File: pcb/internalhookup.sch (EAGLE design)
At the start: 8 parts, among them CN1 LASER, J1 CONTROL, J2 SERVO, J4 AZIMUTH, Q2 SMMBT2222ALT, U1 AMS1117-3.3

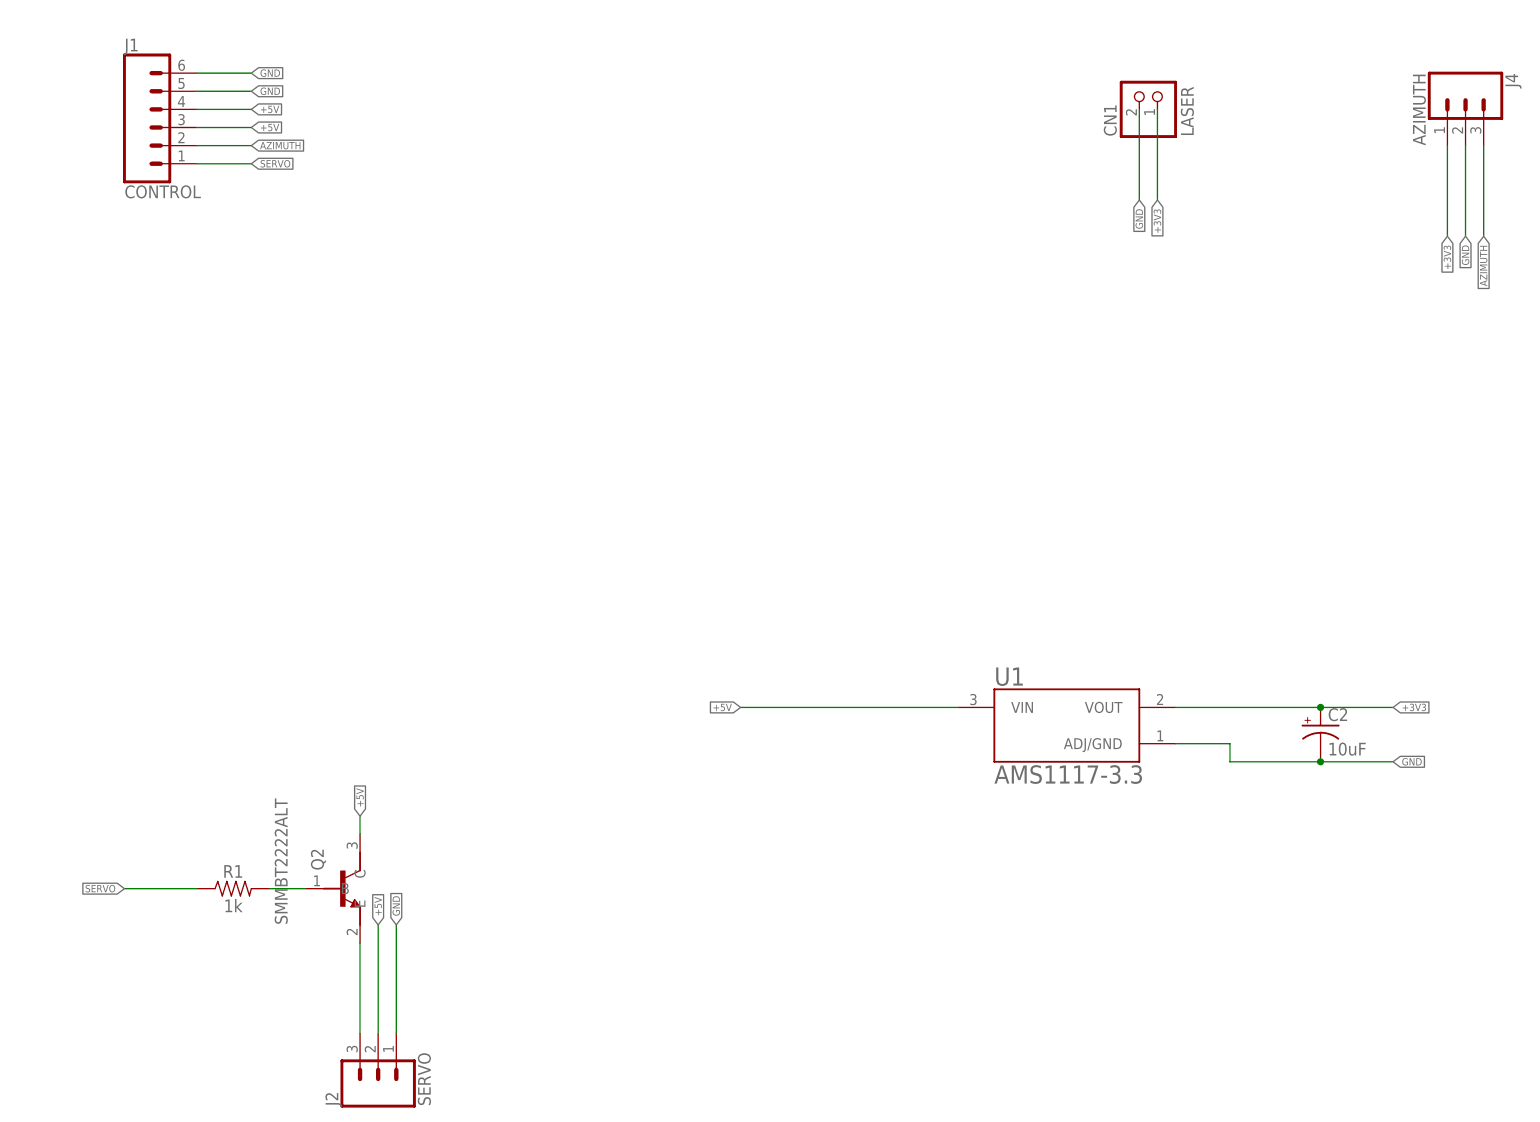
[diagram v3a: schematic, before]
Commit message: Hookup board revision to 1.6
* Added a cap in front of the servo as the line to get the 5V is long
and may not be totally reliable under stress
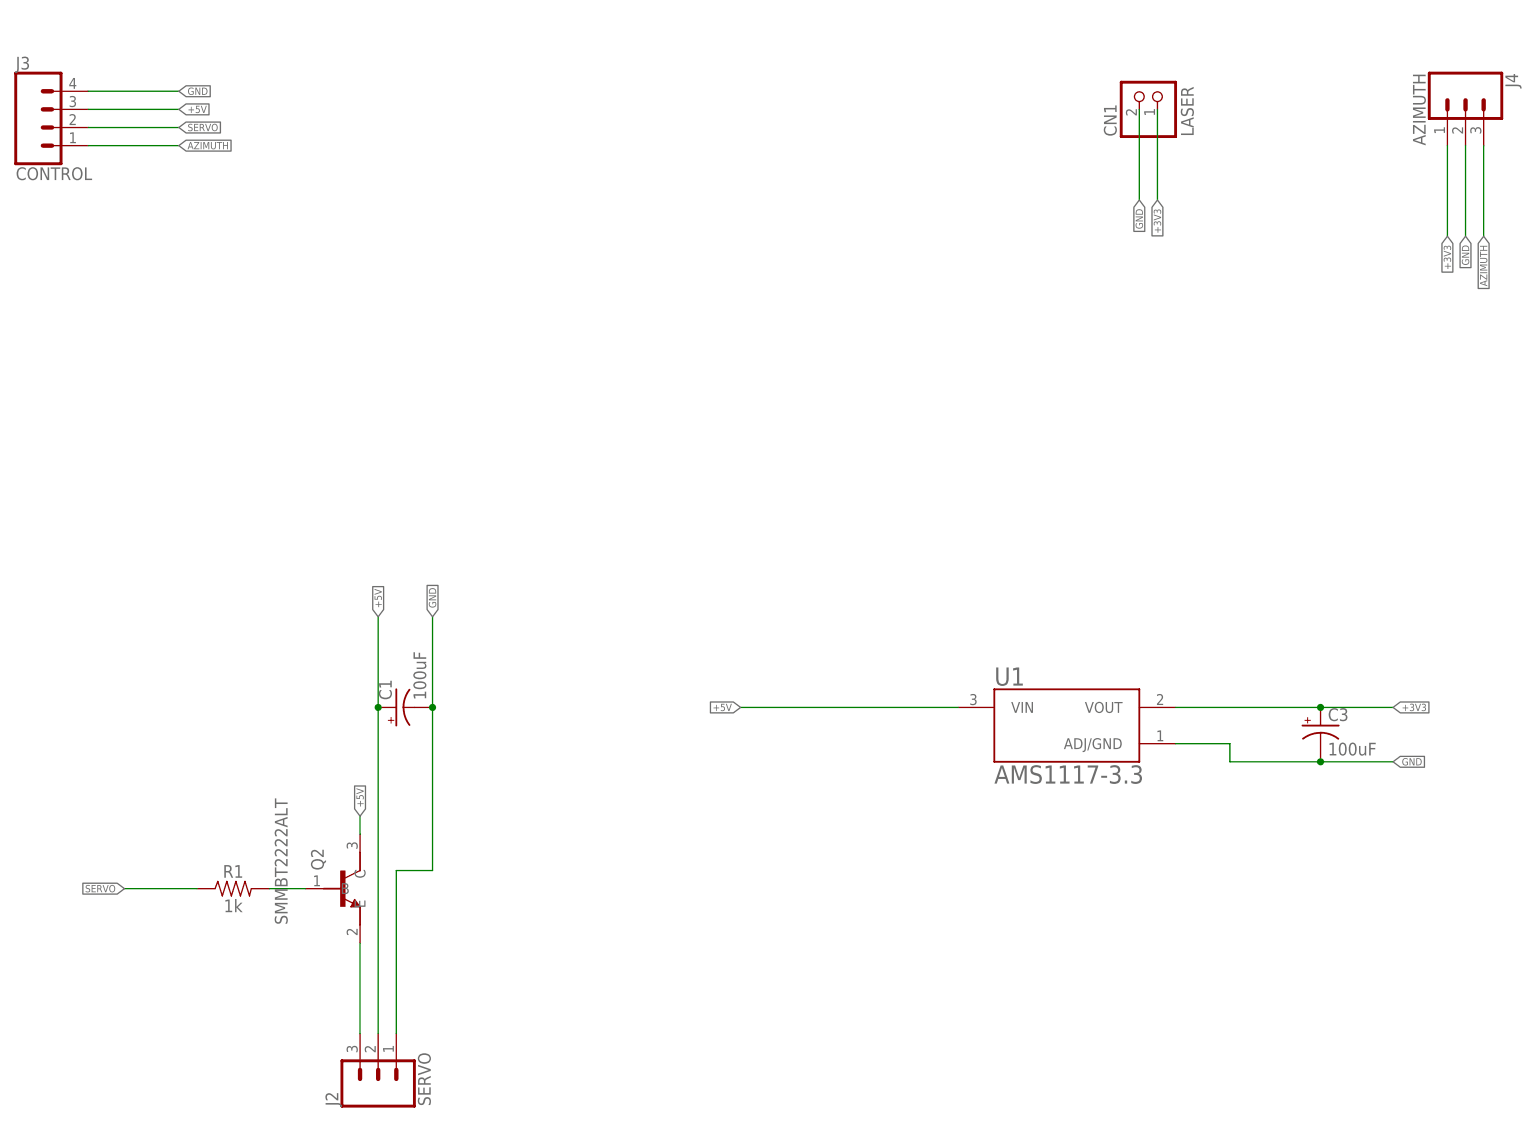
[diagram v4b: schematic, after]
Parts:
- removed C2: 10uF, SparkFun-Capacitors:10UF-POLAR-RADIAL-2.5MM-25V-20%
- removed J1: CONTROL, SparkFun-Connectors:CONN_06SILK_FEMALE_PTH
- added C1, C3: 100uF, SparkFun-Capacitors:100UF-POLAR-RADIAL-2.5MM-25V-20%
- added J3: CONTROL, SparkFun-Connectors:CONN_04
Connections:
- net +3V3: now also C3.+; no longer C2.+
- net +5V: now also C1.+, J3.3; no longer J1.3, J1.4
- net AZIMUTH: now also J3.1; no longer J1.2
- net GND: now also C1.-, C3.-, J3.4; no longer C2.-, J1.5, J1.6
- net SERVO: now also J3.2; no longer J1.1
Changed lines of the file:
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@@
 <part name="CN1" library="adafruit" library_urn="urn:adsk.eagle:library:420" deviceset="JST_2PIN" device="-THM-RA" package3d_urn="urn:adsk.eagle:package:6240694/1" value=" LASER"/>
 <part name="U1" library="AMS1117-3.3" deviceset="AMS1117-3.3" device=""/>
-<part name="C2" library="SparkFun-Capacitors" library_urn="urn:adsk.eagle:library:510" deviceset="10UF-POLAR" device="-RADIAL-2.5MM-25V-20%" package3d_urn="urn:adsk.eagle:package:37423/1" value="10uF"/>
 <part name="Q2" library="MMBT3904" deviceset="MMBT3904" device="" value="SMMBT2222ALT"/>
-<part name="J1" library="SparkFun-Connectors" library_urn="urn:adsk.eagle:library:513" deviceset="CONN_06" device="SILK_FEMALE_PTH" package3d_urn="urn:adsk.eagle:package:38009/1" value="CONTROL"/>
 <part name="J4" library="SparkFun-Connectors" library_urn="urn:adsk.eagle:library:513" deviceset="CONN_03" device="" package3d_urn="urn:adsk.eagle:package:38063/1" value="AZIMUTH"/>
+<part name="J3" library="SparkFun-Connectors" library_urn="urn:adsk.eagle:library:513" deviceset="CONN_04" device="" package3d_urn="urn:adsk.eagle:package:38085/1" value="CONTROL"/>
+<part name="C1" library="SparkFun-Capacitors" library_urn="urn:adsk.eagle:library:510" deviceset="100UF-POLAR" device="-RADIAL-2.5MM-25V-20%" package3d_urn="urn:adsk.eagle:package:37415/1" value="100uF"/>
+<part name="C3" library="SparkFun-Capacitors" library_urn="urn:adsk.eagle:library:510" deviceset="100UF-POLAR" device="-RADIAL-2.5MM-25V-20%" package3d_urn="urn:adsk.eagle:package:37415/1" value="100uF"/>
 </parts>
 <sheets>
@@
 <attribute name="VALUE" x="152.3908" y="85.844640625" size="2.5423" layer="96"/>
 </instance>
-<instance part="C2" gate="G$1" x="198.12" y="93.98" smashed="yes">
-<attribute name="NAME" x="199.136" y="94.615" size="1.778" layer="95" font="vector"/>
-<attribute name="VALUE" x="199.136" y="89.789" size="1.778" layer="96" font="vector"/>
-</instance>
 <instance part="Q2" gate="G$1" x="60.96" y="71.12" smashed="yes">
 <attribute name="NAME" x="58.42" y="73.663840625" size="1.779340625" layer="95" rot="R90"/>
 <attribute name="VALUE" x="53.34501875" y="66.050040625" size="1.781509375" layer="96" rot="R90"/>
 </instance>
-<instance part="J1" gate="G$1" x="35.56" y="177.8" smashed="yes">
-<attribute name="VALUE" x="30.48" y="167.894" size="1.778" layer="96" font="vector"/>
-<attribute name="NAME" x="30.48" y="188.468" size="1.778" layer="95" font="vector"/>
-</instance>
 <instance part="J4" gate="J$1" x="218.44" y="182.88" smashed="yes" rot="R270">
 <attribute name="VALUE" x="211.074" y="185.42" size="1.778" layer="96" font="vector" rot="R270"/>
 <attribute name="NAME" x="224.028" y="185.42" size="1.778" layer="95" font="vector" rot="R270"/>
+</instance>
+<instance part="J3" gate="G$1" x="20.32" y="177.8" smashed="yes">
+<attribute name="VALUE" x="15.24" y="170.434" size="1.778" layer="96" font="vector"/>
+<attribute name="NAME" x="15.24" y="185.928" size="1.778" layer="95" font="vector"/>
+</instance>
+<instance part="C1" gate="G$1" x="68.58" y="96.52" smashed="yes" rot="R90">
+<attribute name="NAME" x="67.945" y="97.536" size="1.778" layer="95" font="vector" rot="R90"/>
+<attribute name="VALUE" x="72.771" y="97.536" size="1.778" layer="96" font="vector" rot="R90"/>
+</instance>
+<instance part="C3" gate="G$1" x="198.12" y="93.98" smashed="yes">
+<attribute name="NAME" x="199.136" y="94.615" size="1.778" layer="95" font="vector"/>
+<attribute name="VALUE" x="199.136" y="89.789" size="1.778" layer="96" font="vector"/>
 </instance>
 </instances>
@@
 <net name="GND" class="0">
 <segment>
-<pinref part="J2" gate="J$1" pin="1"/>
-<wire x1="68.58" y1="50.8" x2="68.58" y2="66.04" width="0.1524" layer="91"/>
-<label x="68.58" y="66.04" size="1.016" layer="95" rot="R90" xref="yes"/>
-</segment>
-<segment>
 <wire x1="177.8" y1="91.44" x2="185.42" y2="91.44" width="0.1524" layer="91"/>
 <wire x1="185.42" y1="91.44" x2="185.42" y2="88.9" width="0.1524" layer="91"/>
@@
 <label x="208.28" y="88.9" size="1.016" layer="95" xref="yes"/>
 <pinref part="U1" gate="G$1" pin="ADJ/GND"/>
-<pinref part="C2" gate="G$1" pin="-"/>
+<pinref part="C3" gate="G$1" pin="-"/>
 <wire x1="198.12" y1="88.9" x2="208.28" y2="88.9" width="0.1524" layer="91"/>
 <junction x="198.12" y="88.9"/>
 </segment>
 <segment>
-<wire x1="40.64" y1="185.42" x2="48.26" y2="185.42" width="0.1524" layer="91"/>
-<label x="48.26" y="185.42" size="1.016" layer="95" xref="yes"/>
-<pinref part="J1" gate="G$1" pin="6"/>
+<wire x1="25.4" y1="182.88" x2="38.1" y2="182.88" width="0.1524" layer="91"/>
+<label x="38.1" y="182.88" size="1.016" layer="95" xref="yes"/>
+<pinref part="J3" gate="G$1" pin="4"/>
 </segment>
 <segment>
@@
 </segment>
 <segment>
-<wire x1="40.64" y1="182.88" x2="48.26" y2="182.88" width="0.1524" layer="91"/>
-<label x="48.26" y="182.88" size="1.016" layer="95" xref="yes"/>
-<pinref part="J1" gate="G$1" pin="5"/>
+<pinref part="J2" gate="J$1" pin="1"/>
+<wire x1="68.58" y1="50.8" x2="68.58" y2="73.66" width="0.1524" layer="91"/>
+<pinref part="C1" gate="G$1" pin="-"/>
+<wire x1="68.58" y1="73.66" x2="73.66" y2="73.66" width="0.1524" layer="91"/>
+<wire x1="73.66" y1="73.66" x2="73.66" y2="96.52" width="0.1524" layer="91"/>
+<wire x1="73.66" y1="96.52" x2="73.66" y2="109.22" width="0.1524" layer="91"/>
+<junction x="73.66" y="96.52"/>
+<label x="73.66" y="109.22" size="1.016" layer="95" rot="R90" xref="yes"/>
 </segment>
 </net>
@@
 </segment>
 <segment>
-<pinref part="J2" gate="J$1" pin="2"/>
-<wire x1="66.04" y1="50.8" x2="66.04" y2="66.04" width="0.1524" layer="91"/>
-<label x="66.04" y="66.04" size="1.016" layer="95" rot="R90" xref="yes"/>
+<wire x1="25.4" y1="180.34" x2="38.1" y2="180.34" width="0.1524" layer="91"/>
+<label x="38.1" y="180.34" size="1.016" layer="95" xref="yes"/>
+<pinref part="J3" gate="G$1" pin="3"/>
 </segment>
 <segment>
-<pinref part="J1" gate="G$1" pin="4"/>
-<wire x1="40.64" y1="180.34" x2="48.26" y2="180.34" width="0.1524" layer="91"/>
-<label x="48.26" y="180.34" size="1.016" layer="95" xref="yes"/>
-</segment>
-<segment>
-<wire x1="40.64" y1="177.8" x2="48.26" y2="177.8" width="0.1524" layer="91"/>
-<label x="48.26" y="177.8" size="1.016" layer="95" xref="yes"/>
-<pinref part="J1" gate="G$1" pin="3"/>
+<pinref part="J2" gate="J$1" pin="2"/>
+<pinref part="C1" gate="G$1" pin="+"/>
+<wire x1="66.04" y1="50.8" x2="66.04" y2="96.52" width="0.1524" layer="91"/>
+<wire x1="66.04" y1="96.52" x2="66.04" y2="109.22" width="0.1524" layer="91"/>
+<junction x="66.04" y="96.52"/>
+<label x="66.04" y="109.22" size="1.016" layer="95" rot="R90" xref="yes"/>
 </segment>
 </net>
@@
 <segment>
 <label x="208.28" y="96.52" size="1.016" layer="95" xref="yes"/>
+<pinref part="U1" gate="G$1" pin="VOUT"/>
 <wire x1="208.28" y1="96.52" x2="198.12" y2="96.52" width="0.1524" layer="91"/>
-<pinref part="U1" gate="G$1" pin="VOUT"/>
-<pinref part="C2" gate="G$1" pin="+"/>
+<pinref part="C3" gate="G$1" pin="+"/>
 <wire x1="198.12" y1="96.52" x2="177.8" y2="96.52" width="0.1524" layer="91"/>
 <junction x="198.12" y="96.52"/>
@@
 </segment>
 <segment>
-<pinref part="J1" gate="G$1" pin="1"/>
-<wire x1="40.64" y1="172.72" x2="48.26" y2="172.72" width="0.1524" layer="91"/>
-<label x="48.26" y="172.72" size="1.016" layer="95" xref="yes"/>
+<wire x1="25.4" y1="177.8" x2="38.1" y2="177.8" width="0.1524" layer="91"/>
+<label x="38.1" y="177.8" size="1.016" layer="95" xref="yes"/>
+<pinref part="J3" gate="G$1" pin="2"/>
 </segment>
 </net>
@@
 </segment>
 <segment>
-<pinref part="J1" gate="G$1" pin="2"/>
-<wire x1="40.64" y1="175.26" x2="48.26" y2="175.26" width="0.1524" layer="91"/>
-<label x="48.26" y="175.26" size="1.016" layer="95" xref="yes"/>
+<wire x1="25.4" y1="175.26" x2="38.1" y2="175.26" width="0.1524" layer="91"/>
+<label x="38.1" y="175.26" size="1.016" layer="95" xref="yes"/>
+<pinref part="J3" gate="G$1" pin="1"/>
 </segment>
 </net>
